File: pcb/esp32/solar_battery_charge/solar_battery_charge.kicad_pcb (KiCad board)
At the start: 2 copper layers, 12 parts, among them J1 USB_A, J2 Conn_01x02_Female, J3 Conn_01x02_Female, J4 Screw_Terminal_01x02, J5 Conn_01x02_Female, J6 Conn_01x02_Female, J7 Conn_01x01_Male, J8 Conn_01x01_Male, U1 LM7805_TO220, U2 MCP1700-1202E_TO92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

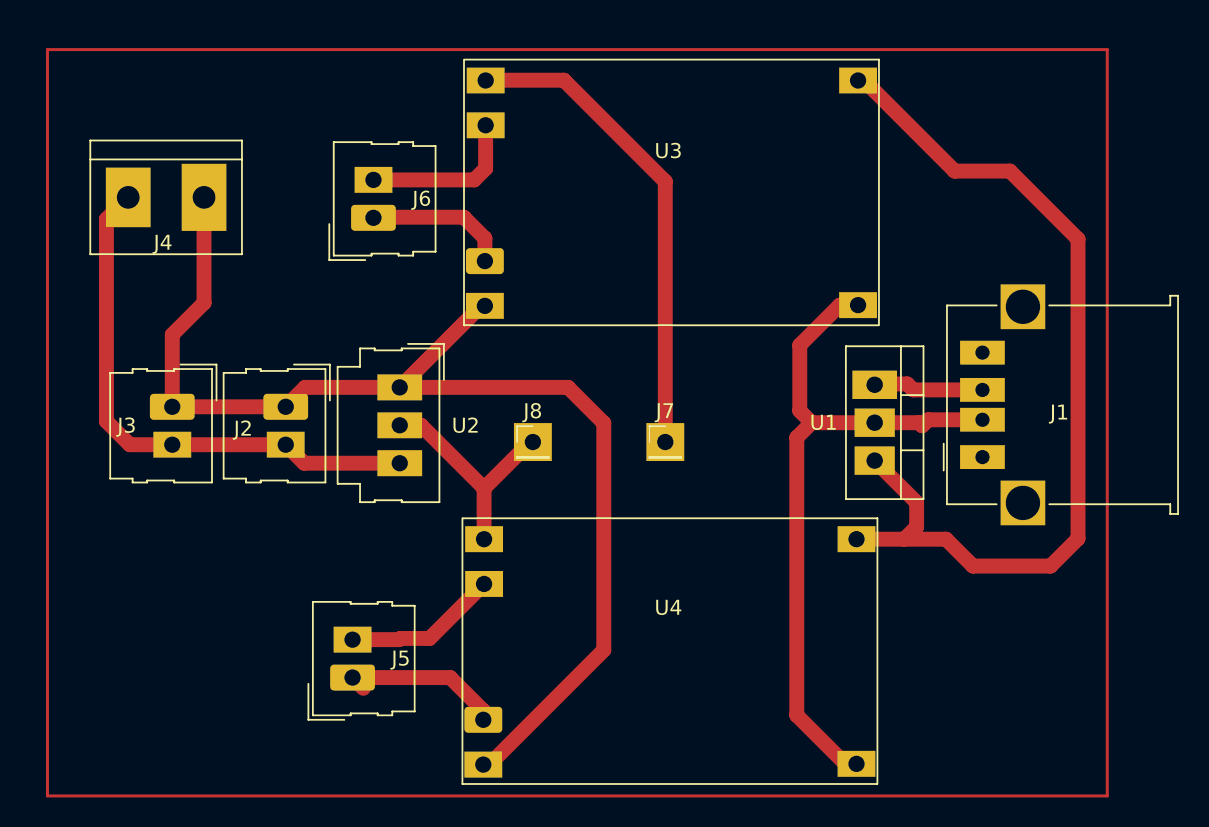
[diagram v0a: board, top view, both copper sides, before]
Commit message: updated solar baterry charge pcb, by changing lm7805 for ams1117 voltage regulator, also repositioned the layout
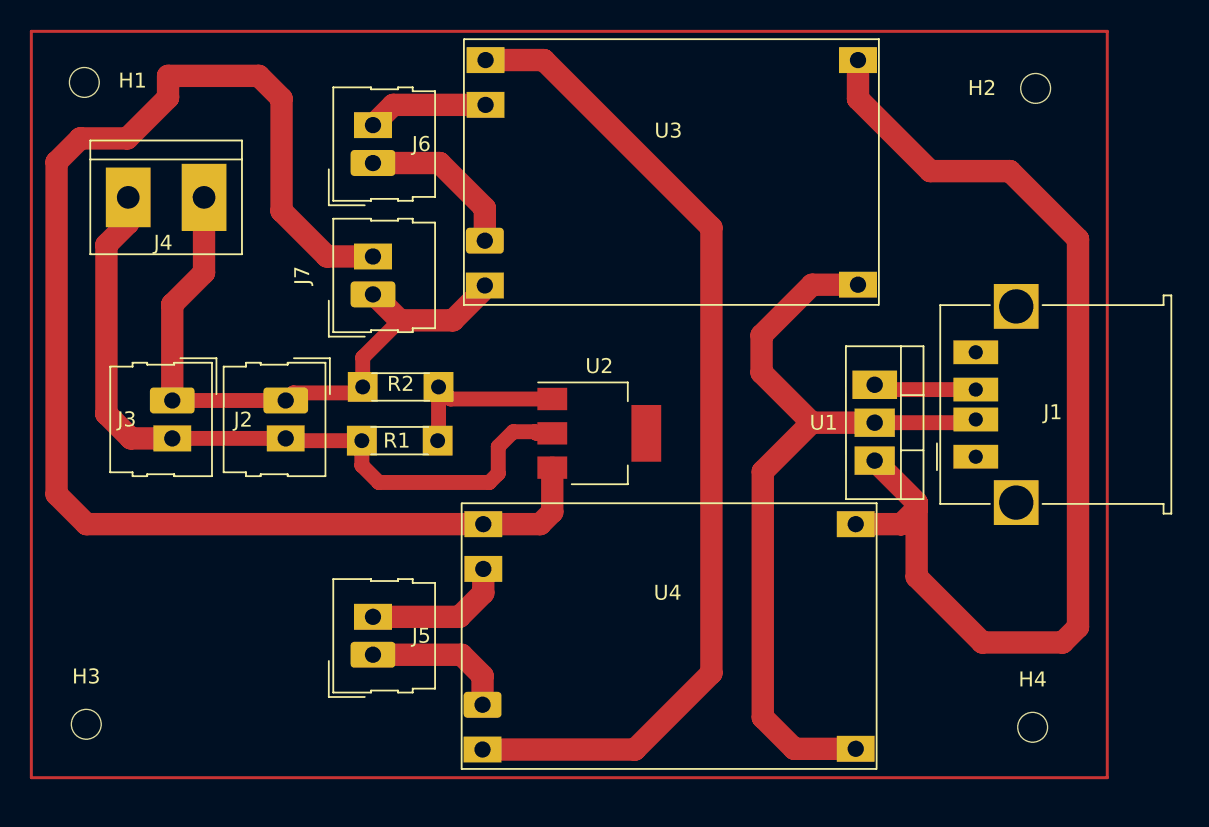
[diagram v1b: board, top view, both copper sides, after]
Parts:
- removed J8: Conn_01x01_Male, Connector_PinHeader_2.00mm:PinHeader_1x01_P2.00mm_Vertical
- added H1: MountingHole, MountingHole:MountingHole_2mm, F.Cu at (100.1, 27.8)
- added H2: MountingHole, MountingHole:MountingHole_2mm, F.Cu at (163.8, 28.2)
- added H3: MountingHole, MountingHole:MountingHole_2mm, F.Cu at (100.2, 70.8)
- added H4: MountingHole, MountingHole:MountingHole_2mm, F.Cu at (163.6, 71.0)
- added R1: R, Resistor_THT:R_Axial_DIN0204_L3.6mm_D1.6mm_P5.08mm_Horizontal, F.Cu at (118.7, 51.8)
- added R2: R, Resistor_THT:R_Axial_DIN0204_L3.6mm_D1.6mm_P5.08mm_Horizontal, F.Cu at (123.8, 48.2)
- J2: value Conn_01x02_Female -> capacitor2
- J7: value Conn_01x01_Male -> capacitor1; footprint Connector_PinHeader_2.00mm:PinHeader_1x01_P2.00mm_Vertical -> smart_sensor:Connector_Molex_Molex_SL_171971-0004_1x02_P2.54mm_Vertical_squares
- U2: value MCP1700-1202E_TO92 -> LM1117-ADJ; footprint smart_sensor:Connector_Molex__Molex_SL_171971-0003_1x03_P2.54mm_Vertical -> Package_TO_SOT_SMD:SOT-223-3_TabPin2
- moved J7 26.3 mm to (115.2, 40.7), turned to 90 degrees
- moved U2 9.46 mm to (134.6, 51.3), turned to 0 degrees
- moved J6 3.67 mm to (115.2, 31.9)
- moved J5 2.05 mm to (115.2, 64.9)
- moved U3 1.37 mm to (139.5, 30.9)
- moved U4 1.01 mm to (139.3, 62.0)
- moved J1 0.45 mm to (170.5, 50.1)
- moved J2 0.42 mm to (117.8, 50.4)
- moved J3 0.42 mm to (110.2, 50.4)
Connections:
- J2 pad 2: 3.3v -> 5.0v_bat
- J3 pad 2: 3.3v -> 5.0v_bat
- J4 pad 2: 3.3v -> 5.0v_bat
- J7 pad 1: battery+ -> battery-
- U2 pad 1: battery- -> Net-(R1-Pad2)
- U2 pad 2: battery+ -> 5.0v_bat
- U2 pad 3: 3.3v -> battery+
- U3 pad 4: battery+ -> battery_series
- U4 pad 3: battery- -> battery_series
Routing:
- net battery_series: track 0.00 -> 67.1 mm
- net 5.0v_bat: track 0.00 -> 50.4 mm
- net battery+: track 47.7 -> 93.5 mm
- net battery-: track 79.8 -> 42.4 mm
- net 3.3v: track 36.4 -> 0.00 mm
- net 5v+: track 62.3 -> 74.2 mm
- net Net-(R1-Pad2): track 0.00 -> 11.6 mm
- net solarPanel-: track 47.6 -> 54.5 mm
- net batery2+: track 11.0 -> 8.12 mm
- net batery1-: track 11.3 -> 9.87 mm
- net batery2-: track 9.59 -> 10.9 mm
- net batery1+: track 10.4 -> 9.66 mm

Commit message: added diode to esp32 board and updated solar board to fixed 5.0v ams1117
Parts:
- removed R1, R2: R, Resistor_THT:R_Axial_DIN0204_L3.6mm_D1.6mm_P5.08mm_Horizontal
- U2: value LM1117-ADJ -> LM1117-5.0
- moved J7 27.9 mm to (141.2, 50.8), turned to -90 degrees
- moved U2 9.46 mm to (125.2, 50.0)
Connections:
- U2 pad 1: Net-(R1-Pad2) -> battery-
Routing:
- net battery+: track 93.5 -> 31.5 mm
- net battery-: track 42.4 -> 66.1 mm
- net 5.0v_bat: track 50.4 -> 37.2 mm
- net Net-(R1-Pad2): track 11.6 -> 0.00 mm

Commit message: added 2 pairs of male pins to measure solar panel voltage and battery voltage
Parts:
- added J8: solar_panel_measure_voltage, smart_sensor:Connector_Molex_Molex_SL_171971-0004_1x02_P2.54mm_Vertical_squares, F.Cu at (167.1, 36.2)
- added J9: measure_battery_voltage, smart_sensor:Connector_Molex_Molex_SL_171971-0004_1x02_P2.54mm_Vertical_squares, F.Cu at (134.9, 50.0)
- moved J3 3.99 mm to (106.2, 50.3)
- moved U2 3.99 mm to (121.2, 50.0)
- moved J2 3.99 mm to (113.8, 50.3)
- moved J7 1.86 mm to (142.9, 50.0)
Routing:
- net solarPanel+: track 7.37 -> 25.4 mm
- net solarPanel-: track 54.5 -> 66.8 mm
- net battery+: track 31.5 -> 41.5 mm
- net battery-: track 66.1 -> 74.7 mm
- net 5v+: track 74.2 -> 79.3 mm
- net battery_series: track 67.1 -> 69.3 mm
- net 5.0v_bat: track 37.2 -> 38.3 mm

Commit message: added new pins to connect more 3.3v sensors and 5.0v sensors, also added 2 pull up resistors for sda and scl pins
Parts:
- moved J5 2.87 mm to (112.3, 65.2)
- moved J6 1.89 mm to (114.9, 33.8)
- moved U3 0.71 mm to (139.4, 30.2)
- moved U4 0.59 mm to (139.4, 61.4)
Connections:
- J1 pad 1: unconnected-(J1-Pad1) -> solarPanel+
- J1 pad 2: solarPanel- -> unconnected-(J1-Pad2)
- J1 pad 3: solarPanel+ -> unconnected-(J1-Pad3)
- J1 pad 4: unconnected-(J1-Pad4) -> solarPanel-
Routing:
- net solarPanel+: track 25.4 -> 40.0 mm
- net 5v+: track 79.3 -> 82.6 mm
- net batery2-: track 10.9 -> 8.60 mm
- net battery_series: track 69.3 -> 71.4 mm
- net batery1+: track 9.66 -> 11.3 mm
- net batery1-: track 9.87 -> 11.1 mm
- net battery-: track 74.7 -> 75.8 mm
- net battery+: track 41.5 -> 42.2 mm
